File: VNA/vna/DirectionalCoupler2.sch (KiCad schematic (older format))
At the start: 6 parts

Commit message: adjusted main schematic to suit initial presentation
i moved a few blocks around so that the cropped version of the block diagram would fit nicely in my semester 1 presentation
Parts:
- renumbered L1 to L5, L3 to L6, L2 to L7, L4 to L8, R1 to R3, R2 to R4
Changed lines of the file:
@@
 k1 l5 l6 0.999
 $Comp
-L Device:L L2
+L Device:L L?
 U 1 1 5CC70FE5
 P 5000 3300
-AR Path="/5CC1CC6B/5CC70FE5" Ref="L2"  Part="1"
-AR Path="/5CC2F156/5CC70FE5" Ref="L6"  Part="1"
+AR Path="/5CC1CC6B/5CC70FE5" Ref="L?"  Part="1"
+AR Path="/5CC2F156/5CC70FE5" Ref="L?"  Part="1"
 AR Path="/5CC6A089/5CC70FE5" Ref="L7"  Part="1"
 F 0 "L7" V 4950 3200 50  0000 C CNN
@@
 $EndComp
 $Comp
-L Device:L L4
+L Device:L L?
 U 1 1 5CC70FE6
 P 5800 3500
-AR Path="/5CC1CC6B/5CC70FE6" Ref="L4"  Part="1"
-AR Path="/5CC2F156/5CC70FE6" Ref="L8"  Part="1"
+AR Path="/5CC1CC6B/5CC70FE6" Ref="L?"  Part="1"
+AR Path="/5CC2F156/5CC70FE6" Ref="L?"  Part="1"
 AR Path="/5CC6A089/5CC70FE6" Ref="L8"  Part="1"
 F 0 "L8" V 5850 3350 50  0000 C CNN
@@
 	5650 3300 5650 3500
 $Comp
-L power:GND #PWR04
+L power:GND #PWR?
 U 1 1 5CC70FE7
 P 5950 3250
-AR Path="/5CC1CC6B/5CC70FE7" Ref="#PWR04"  Part="1"
-AR Path="/5CC2F156/5CC70FE7" Ref="#PWR07"  Part="1"
-AR Path="/5CC6A089/5CC70FE7" Ref="#PWR0101"  Part="1"
-F 0 "#PWR0101" H 5950 3000 50  0001 C CNN
+AR Path="/5CC1CC6B/5CC70FE7" Ref="#PWR?"  Part="1"
+AR Path="/5CC2F156/5CC70FE7" Ref="#PWR?"  Part="1"
+AR Path="/5CC6A089/5CC70FE7" Ref="#PWR06"  Part="1"
+F 0 "#PWR06" H 5950 3000 50  0001 C CNN
 F 1 "GND" H 6050 3150 50  0000 C CNN
 F 2 "" H 5950 3250 50  0001 C CNN
@@
 $EndComp
 $Comp
-L Device:R_Small_US R2
+L Device:R_Small_US R?
 U 1 1 5CC70FE8
 P 5950 3700
-AR Path="/5CC1CC6B/5CC70FE8" Ref="R2"  Part="1"
-AR Path="/5CC2F156/5CC70FE8" Ref="R4"  Part="1"
+AR Path="/5CC1CC6B/5CC70FE8" Ref="R?"  Part="1"
+AR Path="/5CC2F156/5CC70FE8" Ref="R?"  Part="1"
 AR Path="/5CC6A089/5CC70FE8" Ref="R4"  Part="1"
 F 0 "R4" H 6018 3746 50  0000 L CNN
@@
 $EndComp
 $Comp
-L Device:R_Small_US R1
+L Device:R_Small_US R?
 U 1 1 5CC2B8C4
 P 4850 3500
-AR Path="/5CC1CC6B/5CC2B8C4" Ref="R1"  Part="1"
-AR Path="/5CC2F156/5CC2B8C4" Ref="R3"  Part="1"
+AR Path="/5CC1CC6B/5CC2B8C4" Ref="R?"  Part="1"
+AR Path="/5CC2F156/5CC2B8C4" Ref="R?"  Part="1"
 AR Path="/5CC6A089/5CC2B8C4" Ref="R3"  Part="1"
 F 0 "R3" H 4918 3546 50  0000 L CNN
@@
 Connection ~ 5950 3500
 $Comp
-L power:GND #PWR03
+L power:GND #PWR?
 U 1 1 5CC2B8D0
 P 4850 3600
-AR Path="/5CC1CC6B/5CC2B8D0" Ref="#PWR03"  Part="1"
-AR Path="/5CC2F156/5CC2B8D0" Ref="#PWR06"  Part="1"
-AR Path="/5CC6A089/5CC2B8D0" Ref="#PWR0102"  Part="1"
-F 0 "#PWR0102" H 4850 3350 50  0001 C CNN
+AR Path="/5CC1CC6B/5CC2B8D0" Ref="#PWR?"  Part="1"
+AR Path="/5CC2F156/5CC2B8D0" Ref="#PWR?"  Part="1"
+AR Path="/5CC6A089/5CC2B8D0" Ref="#PWR07"  Part="1"
+F 0 "#PWR07" H 4850 3350 50  0001 C CNN
 F 1 "GND" H 4950 3500 50  0000 C CNN
 F 2 "" H 4850 3600 50  0001 C CNN
@@
 $EndComp
 $Comp
-L power:GND #PWR05
+L power:GND #PWR?
 U 1 1 5CC2B8D6
 P 5950 3800
-AR Path="/5CC1CC6B/5CC2B8D6" Ref="#PWR05"  Part="1"
-AR Path="/5CC2F156/5CC2B8D6" Ref="#PWR08"  Part="1"
-AR Path="/5CC6A089/5CC2B8D6" Ref="#PWR0103"  Part="1"
-F 0 "#PWR0103" H 5950 3550 50  0001 C CNN
+AR Path="/5CC1CC6B/5CC2B8D6" Ref="#PWR?"  Part="1"
+AR Path="/5CC2F156/5CC2B8D6" Ref="#PWR?"  Part="1"
+AR Path="/5CC6A089/5CC2B8D6" Ref="#PWR08"  Part="1"
+F 0 "#PWR08" H 5950 3550 50  0001 C CNN
 F 1 "GND" H 6050 3700 50  0000 C CNN
 F 2 "" H 5950 3800 50  0001 C CNN
@@
 $EndComp
 $Comp
-L Device:L L1
+L Device:L L?
 U 1 1 5CC2B8DC
 P 5000 3050
-AR Path="/5CC1CC6B/5CC2B8DC" Ref="L1"  Part="1"
-AR Path="/5CC2F156/5CC2B8DC" Ref="L5"  Part="1"
+AR Path="/5CC1CC6B/5CC2B8DC" Ref="L?"  Part="1"
+AR Path="/5CC2F156/5CC2B8DC" Ref="L?"  Part="1"
 AR Path="/5CC6A089/5CC2B8DC" Ref="L5"  Part="1"
 F 0 "L5" V 4950 2950 50  0000 C CNN
@@
 $EndComp
 $Comp
-L Device:L L3
+L Device:L L?
 U 1 1 5CC2B8E2
 P 5800 3250
-AR Path="/5CC1CC6B/5CC2B8E2" Ref="L3"  Part="1"
-AR Path="/5CC2F156/5CC2B8E2" Ref="L7"  Part="1"
+AR Path="/5CC1CC6B/5CC2B8E2" Ref="L?"  Part="1"
+AR Path="/5CC2F156/5CC2B8E2" Ref="L?"  Part="1"
 AR Path="/5CC6A089/5CC2B8E2" Ref="L6"  Part="1"
 F 0 "L6" V 5750 3150 50  0000 C CNN

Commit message: changed inductors to a single transformer component
inductors in the directional couplers was changed to a single transformer

this will help with later layout opperations
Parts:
- removed L5, L6, L7, L8: L, symbol Device:L
- removed R3, R4: 50, symbol Device:R_Small_US
- added R? (x2): 50, symbol Device:R_Small_US
- added T? (x2): Transformer_1P_1S, symbol Device:Transformer_1P_1S
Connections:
- net labels added: Fwd1, Rev1
- net labels removed: Fwd2, Rev2
- wire segments 12 -> 16
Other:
- note added: "Pins 1 and 2 of transformer are the coaxial cable, pins 3 and 4 the smaller wire that is wrapped around the toroid.\n\nThe transformer should be wound as a 1:10 ratio"
- note removed: "k1 l3 l4 0.999"
- note removed: "k1 l5 l6 0.999"
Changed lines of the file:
@@
 Comment4 ""
 $EndDescr
-Text Notes 5700 3450 0    50   ~ 0
-k1 l3 l4 0.999
-Text Notes 4750 3200 0    50   ~ 0
-k1 l5 l6 0.999
-$Comp
-L Device:L L?
-U 1 1 5CC70FE5
-P 5000 3300
-AR Path="/5CC1CC6B/5CC70FE5" Ref="L?"  Part="1"
-AR Path="/5CC2F156/5CC70FE5" Ref="L?"  Part="1"
-AR Path="/5CC6A089/5CC70FE5" Ref="L7"  Part="1"
-F 0 "L7" V 4950 3200 50  0000 C CNN
-F 1 "L" V 4950 3400 50  0000 C CNN
-F 2 "" H 5000 3300 50  0001 C CNN
-F 3 "~" H 5000 3300 50  0001 C CNN
-	1    5000 3300
-	0    1    1    0
-$EndComp
-$Comp
-L Device:L L?
-U 1 1 5CC70FE6
-P 5800 3500
-AR Path="/5CC1CC6B/5CC70FE6" Ref="L?"  Part="1"
-AR Path="/5CC2F156/5CC70FE6" Ref="L?"  Part="1"
-AR Path="/5CC6A089/5CC70FE6" Ref="L8"  Part="1"
-F 0 "L8" V 5850 3350 50  0000 C CNN
-F 1 "L" V 5850 3600 50  0000 C CNN
-F 2 "" H 5800 3500 50  0001 C CNN
-F 3 "~" H 5800 3500 50  0001 C CNN
-	1    5800 3500
-	0    1    1    0
-$EndComp
 Wire Wire Line
-	5150 3300 5650 3300
+	6200 3150 6700 3150
 Wire Wire Line
-	5650 3300 5650 3500
+	6700 3150 6700 3350
 $Comp
 L power:GND #PWR?
-U 1 1 5CC70FE7
-P 5950 3250
-AR Path="/5CC1CC6B/5CC70FE7" Ref="#PWR?"  Part="1"
-AR Path="/5CC2F156/5CC70FE7" Ref="#PWR?"  Part="1"
-AR Path="/5CC6A089/5CC70FE7" Ref="#PWR06"  Part="1"
-F 0 "#PWR06" H 5950 3000 50  0001 C CNN
-F 1 "GND" H 6050 3150 50  0000 C CNN
-F 2 "" H 5950 3250 50  0001 C CNN
-F 3 "" H 5950 3250 50  0001 C CNN
-	1    5950 3250
+U 1 1 5CF3F20D
+P 6700 3350
+AR Path="/5CC1CC6B/5CF3F20D" Ref="#PWR?"  Part="1"
+AR Path="/5CC2F156/5CF3F20D" Ref="#PWR?"  Part="1"
+AR Path="/5CC6A089/5CF3F20D" Ref="#PWR?"  Part="1"
+F 0 "#PWR?" H 6700 3100 50  0001 C CNN
+F 1 "GND" H 6800 3250 50  0000 C CNN
+F 2 "" H 6700 3350 50  0001 C CNN
+F 3 "" H 6700 3350 50  0001 C CNN
+	1    6700 3350
 	1    0    0    -1
 $EndComp
 $Comp
 L Device:R_Small_US R?
-U 1 1 5CC70FE8
-P 5950 3700
-AR Path="/5CC1CC6B/5CC70FE8" Ref="R?"  Part="1"
-AR Path="/5CC2F156/5CC70FE8" Ref="R?"  Part="1"
-AR Path="/5CC6A089/5CC70FE8" Ref="R4"  Part="1"
-F 0 "R4" H 6018 3746 50  0000 L CNN
-F 1 "50" H 6018 3655 50  0000 L CNN
-F 2 "" H 5950 3700 50  0001 C CNN
-F 3 "~" H 5950 3700 50  0001 C CNN
-	1    5950 3700
+U 1 1 5CF3F213
+P 6200 4150
+AR Path="/5CC1CC6B/5CF3F213" Ref="R?"  Part="1"
+AR Path="/5CC2F156/5CF3F213" Ref="R?"  Part="1"
+AR Path="/5CC6A089/5CF3F213" Ref="R?"  Part="1"
+F 0 "R?" H 6268 4196 50  0000 L CNN
+F 1 "50" H 6268 4105 50  0000 L CNN
+F 2 "" H 6200 4150 50  0001 C CNN
+F 3 "~" H 6200 4150 50  0001 C CNN
+	1    6200 4150
 	1    0    0    -1
 $EndComp
 $Comp
 L Device:R_Small_US R?
-U 1 1 5CC2B8C4
-P 4850 3500
-AR Path="/5CC1CC6B/5CC2B8C4" Ref="R?"  Part="1"
-AR Path="/5CC2F156/5CC2B8C4" Ref="R?"  Part="1"
-AR Path="/5CC6A089/5CC2B8C4" Ref="R3"  Part="1"
-F 0 "R3" H 4918 3546 50  0000 L CNN
-F 1 "50" H 4918 3455 50  0000 L CNN
-F 2 "" H 4850 3500 50  0001 C CNN
-F 3 "~" H 4850 3500 50  0001 C CNN
-	1    4850 3500
+U 1 1 5CF3F219
+P 4900 3950
+AR Path="/5CC1CC6B/5CF3F219" Ref="R?"  Part="1"
+AR Path="/5CC2F156/5CF3F219" Ref="R?"  Part="1"
+AR Path="/5CC6A089/5CF3F219" Ref="R?"  Part="1"
+F 0 "R?" H 4968 3996 50  0000 L CNN
+F 1 "50" H 4968 3905 50  0000 L CNN
+F 2 "" H 4900 3950 50  0001 C CNN
+F 3 "~" H 4900 3950 50  0001 C CNN
+	1    4900 3950
 	1    0    0    -1
 $EndComp
 Wire Wire Line
-	4850 3300 4800 3300
+	4900 3750 4850 3750
 Wire Wire Line
-	4850 3400 4850 3300
-Connection ~ 4850 3300
+	4900 3850 4900 3750
 Wire Wire Line
-	5950 3500 6000 3500
+	6200 3950 6250 3950
 Wire Wire Line
-	5950 3600 5950 3500
-Connection ~ 5950 3500
+	6200 4050 6200 3950
 $Comp
 L power:GND #PWR?
-U 1 1 5CC2B8D0
-P 4850 3600
-AR Path="/5CC1CC6B/5CC2B8D0" Ref="#PWR?"  Part="1"
-AR Path="/5CC2F156/5CC2B8D0" Ref="#PWR?"  Part="1"
-AR Path="/5CC6A089/5CC2B8D0" Ref="#PWR07"  Part="1"
-F 0 "#PWR07" H 4850 3350 50  0001 C CNN
-F 1 "GND" H 4950 3500 50  0000 C CNN
-F 2 "" H 4850 3600 50  0001 C CNN
-F 3 "" H 4850 3600 50  0001 C CNN
-	1    4850 3600
+U 1 1 5CF3F223
+P 4900 4050
+AR Path="/5CC1CC6B/5CF3F223" Ref="#PWR?"  Part="1"
+AR Path="/5CC2F156/5CF3F223" Ref="#PWR?"  Part="1"
+AR Path="/5CC6A089/5CF3F223" Ref="#PWR?"  Part="1"
+F 0 "#PWR?" H 4900 3800 50  0001 C CNN
+F 1 "GND" H 5000 3950 50  0000 C CNN
+F 2 "" H 4900 4050 50  0001 C CNN
+F 3 "" H 4900 4050 50  0001 C CNN
+	1    4900 4050
 	1    0    0    -1
 $EndComp
 $Comp
 L power:GND #PWR?
-U 1 1 5CC2B8D6
-P 5950 3800
-AR Path="/5CC1CC6B/5CC2B8D6" Ref="#PWR?"  Part="1"
-AR Path="/5CC2F156/5CC2B8D6" Ref="#PWR?"  Part="1"
-AR Path="/5CC6A089/5CC2B8D6" Ref="#PWR08"  Part="1"
-F 0 "#PWR08" H 5950 3550 50  0001 C CNN
-F 1 "GND" H 6050 3700 50  0000 C CNN
-F 2 "" H 5950 3800 50  0001 C CNN
-F 3 "" H 5950 3800 50  0001 C CNN
-	1    5950 3800
+U 1 1 5CF3F229
+P 6200 4250
+AR Path="/5CC1CC6B/5CF3F229" Ref="#PWR?"  Part="1"
+AR Path="/5CC2F156/5CF3F229" Ref="#PWR?"  Part="1"
+AR Path="/5CC6A089/5CF3F229" Ref="#PWR?"  Part="1"
+F 0 "#PWR?" H 6200 4000 50  0001 C CNN
+F 1 "GND" H 6300 4150 50  0000 C CNN
+F 2 "" H 6200 4250 50  0001 C CNN
+F 3 "" H 6200 4250 50  0001 C CNN
+	1    6200 4250
 	1    0    0    -1
 $EndComp
+Wire Wire Line
+	5350 2950 5350 2750
+Wire Wire Line
+	4900 2950 4750 2950
+Wire Wire Line
+	4750 2950 4750 2900
+Wire Wire Line
+	5800 2950 5800 3150
+Wire Wire Line
+	5300 2950 5350 2950
+Wire Wire Line
+	5350 2950 5800 2950
+Connection ~ 5350 2950
+Text HLabel 4850 3750 0    50   Input ~ 0
+Fwd1
+Text HLabel 6250 3950 2    50   Input ~ 0
+Rev1
+Text HLabel 5350 2750 1    50   Input ~ 0
+RFOut
+Text HLabel 4750 2900 0    50   Input ~ 0
+RFIn
 $Comp
-L Device:L L?
-U 1 1 5CC2B8DC
-P 5000 3050
-AR Path="/5CC1CC6B/5CC2B8DC" Ref="L?"  Part="1"
-AR Path="/5CC2F156/5CC2B8DC" Ref="L?"  Part="1"
-AR Path="/5CC6A089/5CC2B8DC" Ref="L5"  Part="1"
-F 0 "L5" V 4950 2950 50  0000 C CNN
-F 1 "L" V 4950 3150 50  0000 C CNN
-F 2 "" H 5000 3050 50  0001 C CNN
-F 3 "~" H 5000 3050 50  0001 C CNN
-	1    5000 3050
-	0    1    1    0
+L Device:Transformer_1P_1S T?
+U 1 1 5CF3F23A
+P 5100 3350
+F 0 "T?" V 5054 3062 50  0000 R CNN
+F 1 "Transformer_1P_1S" V 5145 3062 50  0000 R CNN
+F 2 "" H 5100 3350 50  0001 C CNN
+F 3 "~" H 5100 3350 50  0001 C CNN
+	1    5100 3350
+	0    -1   1    0
 $EndComp
 $Comp
-L Device:L L?
-U 1 1 5CC2B8E2
-P 5800 3250
-AR Path="/5CC1CC6B/5CC2B8E2" Ref="L?"  Part="1"
-AR Path="/5CC2F156/5CC2B8E2" Ref="L?"  Part="1"
-AR Path="/5CC6A089/5CC2B8E2" Ref="L6"  Part="1"
-F 0 "L6" V 5750 3150 50  0000 C CNN
-F 1 "L" V 5750 3400 50  0000 C CNN
-F 2 "" H 5800 3250 50  0001 C CNN
-F 3 "~" H 5800 3250 50  0001 C CNN
-	1    5800 3250
-	0    1    1    0
+L Device:Transformer_1P_1S T?
+U 1 1 5CF3F240
+P 6000 3550
+F 0 "T?" V 6046 3262 50  0000 R CNN
+F 1 "Transformer_1P_1S" V 5955 3262 50  0000 R CNN
+F 2 "" H 6000 3550 50  0001 C CNN
+F 3 "~" H 6000 3550 50  0001 C CNN
+	1    6000 3550
+	0    -1   -1   0
 $EndComp
+Connection ~ 4900 3750
+Connection ~ 6200 3950
 Wire Wire Line
-	5200 3050 5200 2850
+	4900 3750 5150 3750
 Wire Wire Line
-	4850 3050 4700 3050
+	5150 3750 5150 4100
 Wire Wire Line
-	4700 3050 4700 3000
+	5150 4100 5800 4100
 Wire Wire Line
-	5650 3050 5650 3250
-Wire Wire Line
-	5150 3050 5200 3050
-Wire Wire Line
-	5200 3050 5650 3050
-Connection ~ 5200 3050
-Text HLabel 4800 3300 0    50   Input ~ 0
-Fwd2
-Text HLabel 6000 3500 2    50   Input ~ 0
-Rev2
-Text HLabel 5200 2850 1    50   Input ~ 0
-RFOut
-Text HLabel 4700 3000 0    50   Input ~ 0
-RFIn
+	5800 4100 5800 3950
+$Comp
+L power:GND #PWR?
+U 1 1 5CF3F24C
+P 5300 3750
+AR Path="/5CC1CC6B/5CF3F24C" Ref="#PWR?"  Part="1"
+AR Path="/5CC2F156/5CF3F24C" Ref="#PWR?"  Part="1"
+AR Path="/5CC6A089/5CF3F24C" Ref="#PWR?"  Part="1"
+F 0 "#PWR?" H 5300 3500 50  0001 C CNN
+F 1 "GND" H 5400 3650 50  0000 C CNN
+F 2 "" H 5300 3750 50  0001 C CNN
+F 3 "" H 5300 3750 50  0001 C CNN
+	1    5300 3750
+	1    0    0    -1
+$EndComp
+Text Notes 3600 4750 0    50   ~ 0
+Pins 1 and 2 of transformer are the coaxial cable, pins 3 and 4 the smaller wire that is wrapped around the toroid.\n\nThe transformer should be wound as a 1:10 ratio
 $EndSCHEMATC

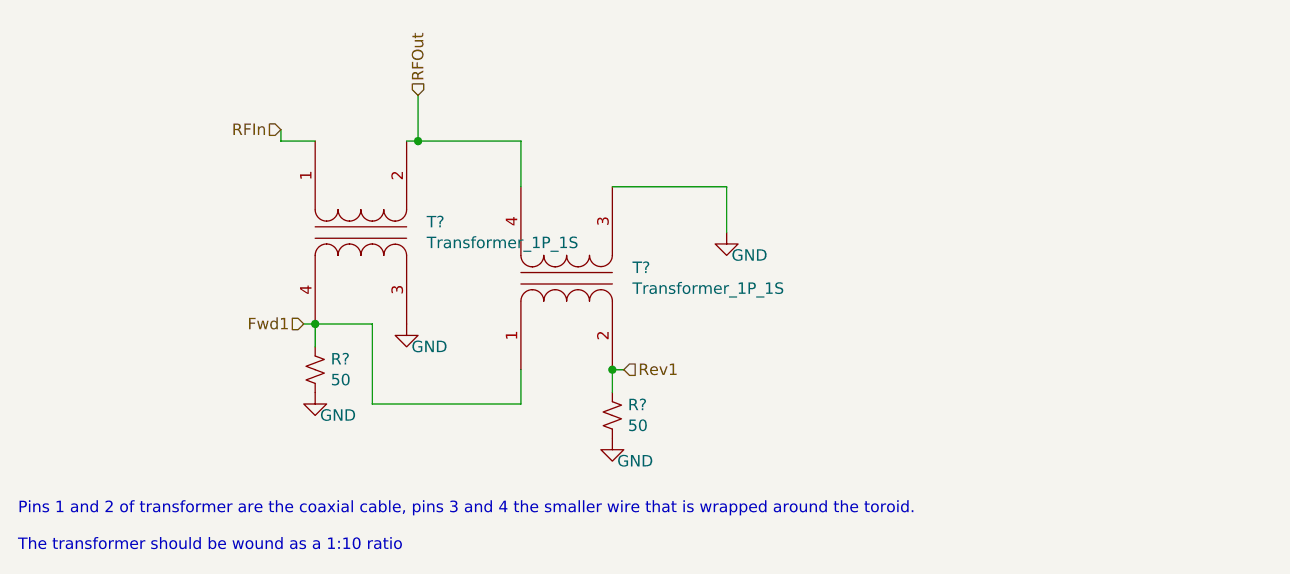
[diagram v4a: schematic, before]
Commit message: micro-controller pins labelled
micro controller pins have been labelled, the pins on the bottom are yet to be linked to them.

still to wire up ftdi chip,

still to decide upon rf switch control schema.
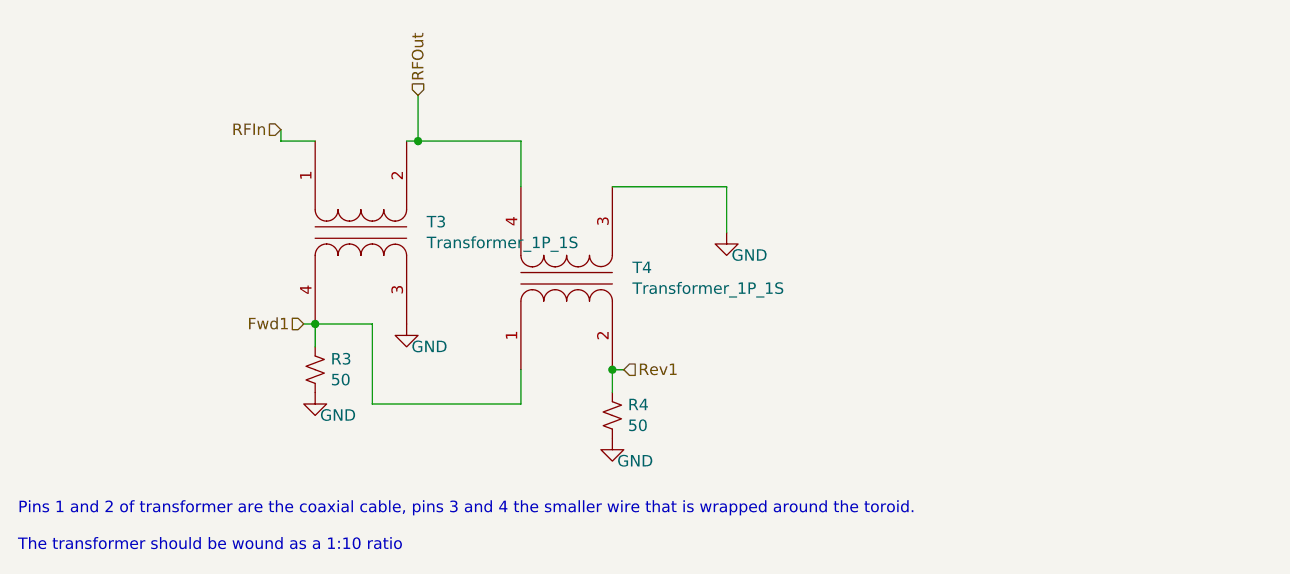
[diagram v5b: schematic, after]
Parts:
- gave numbers to parts that had none: 4
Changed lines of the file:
@@
 AR Path="/5CC1CC6B/5CF3F20D" Ref="#PWR?"  Part="1"
 AR Path="/5CC2F156/5CF3F20D" Ref="#PWR?"  Part="1"
-AR Path="/5CC6A089/5CF3F20D" Ref="#PWR?"  Part="1"
-F 0 "#PWR?" H 6700 3100 50  0001 C CNN
+AR Path="/5CC6A089/5CF3F20D" Ref="#PWR07"  Part="1"
+F 0 "#PWR07" H 6700 3100 50  0001 C CNN
 F 1 "GND" H 6800 3250 50  0000 C CNN
 F 2 "" H 6700 3350 50  0001 C CNN
@@
 AR Path="/5CC1CC6B/5CF3F213" Ref="R?"  Part="1"
 AR Path="/5CC2F156/5CF3F213" Ref="R?"  Part="1"
-AR Path="/5CC6A089/5CF3F213" Ref="R?"  Part="1"
-F 0 "R?" H 6268 4196 50  0000 L CNN
+AR Path="/5CC6A089/5CF3F213" Ref="R4"  Part="1"
+F 0 "R4" H 6268 4196 50  0000 L CNN
 F 1 "50" H 6268 4105 50  0000 L CNN
 F 2 "" H 6200 4150 50  0001 C CNN
@@
 AR Path="/5CC1CC6B/5CF3F219" Ref="R?"  Part="1"
 AR Path="/5CC2F156/5CF3F219" Ref="R?"  Part="1"
-AR Path="/5CC6A089/5CF3F219" Ref="R?"  Part="1"
-F 0 "R?" H 4968 3996 50  0000 L CNN
+AR Path="/5CC6A089/5CF3F219" Ref="R3"  Part="1"
+F 0 "R3" H 4968 3996 50  0000 L CNN
 F 1 "50" H 4968 3905 50  0000 L CNN
 F 2 "" H 4900 3950 50  0001 C CNN
@@
 AR Path="/5CC1CC6B/5CF3F223" Ref="#PWR?"  Part="1"
 AR Path="/5CC2F156/5CF3F223" Ref="#PWR?"  Part="1"
-AR Path="/5CC6A089/5CF3F223" Ref="#PWR?"  Part="1"
-F 0 "#PWR?" H 4900 3800 50  0001 C CNN
+AR Path="/5CC6A089/5CF3F223" Ref="#PWR09"  Part="1"
+F 0 "#PWR09" H 4900 3800 50  0001 C CNN
 F 1 "GND" H 5000 3950 50  0000 C CNN
 F 2 "" H 4900 4050 50  0001 C CNN
@@
 AR Path="/5CC1CC6B/5CF3F229" Ref="#PWR?"  Part="1"
 AR Path="/5CC2F156/5CF3F229" Ref="#PWR?"  Part="1"
-AR Path="/5CC6A089/5CF3F229" Ref="#PWR?"  Part="1"
-F 0 "#PWR?" H 6200 4000 50  0001 C CNN
+AR Path="/5CC6A089/5CF3F229" Ref="#PWR010"  Part="1"
+F 0 "#PWR010" H 6200 4000 50  0001 C CNN
 F 1 "GND" H 6300 4150 50  0000 C CNN
 F 2 "" H 6200 4250 50  0001 C CNN
@@
 RFIn
 $Comp
-L Device:Transformer_1P_1S T?
+L Device:Transformer_1P_1S T3
 U 1 1 5CF3F23A
 P 5100 3350
-F 0 "T?" V 5054 3062 50  0000 R CNN
+F 0 "T3" V 5054 3062 50  0000 R CNN
 F 1 "Transformer_1P_1S" V 5145 3062 50  0000 R CNN
 F 2 "" H 5100 3350 50  0001 C CNN
@@
 $EndComp
 $Comp
-L Device:Transformer_1P_1S T?
+L Device:Transformer_1P_1S T4
 U 1 1 5CF3F240
 P 6000 3550
-F 0 "T?" V 6046 3262 50  0000 R CNN
+F 0 "T4" V 6046 3262 50  0000 R CNN
 F 1 "Transformer_1P_1S" V 5955 3262 50  0000 R CNN
 F 2 "" H 6000 3550 50  0001 C CNN
@@
 AR Path="/5CC1CC6B/5CF3F24C" Ref="#PWR?"  Part="1"
 AR Path="/5CC2F156/5CF3F24C" Ref="#PWR?"  Part="1"
-AR Path="/5CC6A089/5CF3F24C" Ref="#PWR?"  Part="1"
-F 0 "#PWR?" H 5300 3500 50  0001 C CNN
+AR Path="/5CC6A089/5CF3F24C" Ref="#PWR08"  Part="1"
+F 0 "#PWR08" H 5300 3500 50  0001 C CNN
 F 1 "GND" H 5400 3650 50  0000 C CNN
 F 2 "" H 5300 3750 50  0001 C CNN

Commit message: finished controller, chose compatible switches
controller and rf switches have been completed.

ToDo: finish filter design for RF Source, add auto gain control
ToDo: finish directional coupler footprints
ToDo: PCB Layout
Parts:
- R3, R4: footprint (none) -> Resistor_SMD:R_0805_2012Metric_Pad1.15x1.40mm_HandSolder
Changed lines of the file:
@@
 AR Path="/5CC1CC6B/5CF3F20D" Ref="#PWR?"  Part="1"
 AR Path="/5CC2F156/5CF3F20D" Ref="#PWR?"  Part="1"
-AR Path="/5CC6A089/5CF3F20D" Ref="#PWR07"  Part="1"
-F 0 "#PWR07" H 6700 3100 50  0001 C CNN
+AR Path="/5CC6A089/5CF3F20D" Ref="#PWR012"  Part="1"
+F 0 "#PWR012" H 6700 3100 50  0001 C CNN
 F 1 "GND" H 6800 3250 50  0000 C CNN
 F 2 "" H 6700 3350 50  0001 C CNN
@@
 F 0 "R4" H 6268 4196 50  0000 L CNN
 F 1 "50" H 6268 4105 50  0000 L CNN
-F 2 "" H 6200 4150 50  0001 C CNN
+F 2 "Resistor_SMD:R_0805_2012Metric_Pad1.15x1.40mm_HandSolder" H 6200 4150 50  0001 C CNN
 F 3 "~" H 6200 4150 50  0001 C CNN
 	1    6200 4150
@@
 F 0 "R3" H 4968 3996 50  0000 L CNN
 F 1 "50" H 4968 3905 50  0000 L CNN
-F 2 "" H 4900 3950 50  0001 C CNN
+F 2 "Resistor_SMD:R_0805_2012Metric_Pad1.15x1.40mm_HandSolder" H 4900 3950 50  0001 C CNN
 F 3 "~" H 4900 3950 50  0001 C CNN
 	1    4900 3950
@@
 AR Path="/5CC1CC6B/5CF3F223" Ref="#PWR?"  Part="1"
 AR Path="/5CC2F156/5CF3F223" Ref="#PWR?"  Part="1"
-AR Path="/5CC6A089/5CF3F223" Ref="#PWR09"  Part="1"
-F 0 "#PWR09" H 4900 3800 50  0001 C CNN
+AR Path="/5CC6A089/5CF3F223" Ref="#PWR014"  Part="1"
+F 0 "#PWR014" H 4900 3800 50  0001 C CNN
 F 1 "GND" H 5000 3950 50  0000 C CNN
 F 2 "" H 4900 4050 50  0001 C CNN
@@
 AR Path="/5CC1CC6B/5CF3F229" Ref="#PWR?"  Part="1"
 AR Path="/5CC2F156/5CF3F229" Ref="#PWR?"  Part="1"
-AR Path="/5CC6A089/5CF3F229" Ref="#PWR010"  Part="1"
-F 0 "#PWR010" H 6200 4000 50  0001 C CNN
+AR Path="/5CC6A089/5CF3F229" Ref="#PWR015"  Part="1"
+F 0 "#PWR015" H 6200 4000 50  0001 C CNN
 F 1 "GND" H 6300 4150 50  0000 C CNN
 F 2 "" H 6200 4250 50  0001 C CNN
@@
 AR Path="/5CC1CC6B/5CF3F24C" Ref="#PWR?"  Part="1"
 AR Path="/5CC2F156/5CF3F24C" Ref="#PWR?"  Part="1"
-AR Path="/5CC6A089/5CF3F24C" Ref="#PWR08"  Part="1"
-F 0 "#PWR08" H 5300 3500 50  0001 C CNN
+AR Path="/5CC6A089/5CF3F24C" Ref="#PWR013"  Part="1"
+F 0 "#PWR013" H 5300 3500 50  0001 C CNN
 F 1 "GND" H 5400 3650 50  0000 C CNN
 F 2 "" H 5300 3750 50  0001 C CNN
